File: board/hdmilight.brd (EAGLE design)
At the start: 68.5 x 68.6 mm, 73 parts, among them IC1 REG1117, IC2 REG1117, J1 POWER_JACKPTH, Q1 28.6363MHz

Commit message: fixed value of HDMI pull up resistors on receiver board
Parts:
- R1: value 27R -> 27K
- R2, R3: value 47R -> 1K5
- R7, R8: value 47R -> 47K
- R9: value 100R -> 100K
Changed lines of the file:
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@@
 <attribute name="VALUE" x="49.403" y="9.144" size="1.27" layer="27"/>
 </element>
-<element name="R2" library="resistor" package="R0603" value="47R" x="53.086" y="6.35" smashed="yes">
+<element name="R2" library="resistor" package="R0603" value="1K5" x="53.086" y="6.35" smashed="yes">
 <attribute name="NAME" x="52.197" y="7.747" size="1.016" layer="25"/>
 <attribute name="VALUE" x="52.197" y="4.318" size="1.27" layer="27"/>
 </element>
-<element name="R3" library="resistor" package="R0603" value="47R" x="53.086" y="4.064" smashed="yes">
+<element name="R3" library="resistor" package="R0603" value="1K5" x="53.086" y="4.064" smashed="yes">
 <attribute name="NAME" x="52.451" y="1.651" size="1.016" layer="25"/>
 <attribute name="VALUE" x="52.197" y="2.032" size="1.27" layer="27"/>
 </element>
-<element name="R7" library="resistor" package="R0603" value="47R" x="36.068" y="23.622" smashed="yes" rot="R180">
+<element name="R7" library="resistor" package="R0603" value="47K" x="36.068" y="23.622" smashed="yes" rot="R180">
 <attribute name="NAME" x="37.465" y="22.225" size="1.016" layer="25" rot="R180"/>
 <attribute name="VALUE" x="36.957" y="25.654" size="1.27" layer="27" rot="R180"/>
 </element>
-<element name="R8" library="resistor" package="R0603" value="47R" x="36.068" y="25.654" smashed="yes" rot="R180">
+<element name="R8" library="resistor" package="R0603" value="47K" x="36.068" y="25.654" smashed="yes" rot="R180">
 <attribute name="NAME" x="36.703" y="28.321" size="1.016" layer="25" rot="R180"/>
 <attribute name="VALUE" x="36.957" y="27.686" size="1.27" layer="27" rot="R180"/>
 </element>
-<element name="R1" library="resistor" package="R0603" value="27R" x="35.56" y="13.716" smashed="yes" rot="R180">
+<element name="R1" library="resistor" package="R0603" value="27K" x="35.56" y="13.716" smashed="yes" rot="R180">
 <attribute name="NAME" x="32.639" y="14.605" size="1.016" layer="25" rot="R270"/>
 <attribute name="VALUE" x="36.449" y="15.748" size="1.27" layer="27" rot="R180"/>
 </element>
-<element name="R9" library="resistor" package="R0603" value="100R" x="35.56" y="15.748" smashed="yes" rot="R180">
+<element name="R9" library="resistor" package="R0603" value="100K" x="35.56" y="15.748" smashed="yes" rot="R180">
 <attribute name="NAME" x="32.639" y="16.637" size="1.016" layer="25" rot="R270"/>
 <attribute name="VALUE" x="36.449" y="17.78" size="1.27" layer="27" rot="R180"/>

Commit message: added missing capacitor values to schematic
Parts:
- C15, C16, C17, C18, C19, C20, C21, C22, C23, C24, C25, C26, C33, C34, C35, C36, C37: value (none) -> 0.1uF
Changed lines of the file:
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@@
 </element>
 <element name="U$5" library="__SR" package="TSSOP20" value="TXB0108" x="15.748" y="14.986" rot="R270"/>
-<element name="C22" library="resistor" package="C0603" value="" x="41.656" y="24.384" smashed="yes" rot="MR180">
+<element name="C22" library="resistor" package="C0603" value="0.1uF" x="41.656" y="24.384" smashed="yes" rot="MR180">
 <attribute name="NAME" x="40.005" y="23.114" size="1.016" layer="26" rot="MR180"/>
 <attribute name="VALUE" x="40.767" y="26.416" size="1.27" layer="28" rot="MR180"/>
 </element>
-<element name="C15" library="resistor" package="C0402" value="" x="45.466" y="35.052" smashed="yes" rot="MR180">
+<element name="C15" library="resistor" package="C0402" value="0.1uF" x="45.466" y="35.052" smashed="yes" rot="MR180">
 <attribute name="NAME" x="44.323" y="37.084" size="1.016" layer="26" rot="MR180"/>
 <attribute name="VALUE" x="44.831" y="36.957" size="1.27" layer="28" rot="MR180"/>
 </element>
-<element name="C23" library="resistor" package="C0402" value="" x="46.99" y="32.766" smashed="yes" rot="MR90">
+<element name="C23" library="resistor" package="C0402" value="0.1uF" x="46.99" y="32.766" smashed="yes" rot="MR90">
 <attribute name="NAME" x="48.006" y="31.623" size="1.016" layer="26" rot="MR90"/>
 <attribute name="VALUE" x="45.085" y="32.131" size="1.27" layer="28" rot="MR90"/>
 </element>
-<element name="C34" library="resistor" package="C0402" value="" x="40.386" y="35.052" smashed="yes" rot="MR180">
+<element name="C34" library="resistor" package="C0402" value="0.1uF" x="40.386" y="35.052" smashed="yes" rot="MR180">
 <attribute name="NAME" x="39.243" y="37.084" size="1.016" layer="26" rot="MR180"/>
 <attribute name="VALUE" x="39.751" y="36.957" size="1.27" layer="28" rot="MR180"/>
 </element>
-<element name="C16" library="resistor" package="C0603" value="" x="26.67" y="30.734" smashed="yes" rot="MR270">
+<element name="C16" library="resistor" package="C0603" value="0.1uF" x="26.67" y="30.734" smashed="yes" rot="MR270">
 <attribute name="NAME" x="29.21" y="32.131" size="1.016" layer="26" rot="MR270"/>
 <attribute name="VALUE" x="28.702" y="31.623" size="1.27" layer="28" rot="MR270"/>
 </element>
-<element name="C17" library="resistor" package="C0603" value="" x="40.386" y="41.148" smashed="yes" rot="MR0">
+<element name="C17" library="resistor" package="C0603" value="0.1uF" x="40.386" y="41.148" smashed="yes" rot="MR0">
 <attribute name="NAME" x="41.529" y="42.418" size="1.016" layer="26" rot="MR0"/>
 <attribute name="VALUE" x="41.275" y="39.116" size="1.27" layer="28" rot="MR0"/>
 </element>
-<element name="C24" library="resistor" package="C0603" value="" x="49.276" y="39.624" smashed="yes" rot="MR90">
+<element name="C24" library="resistor" package="C0603" value="0.1uF" x="49.276" y="39.624" smashed="yes" rot="MR90">
 <attribute name="NAME" x="50.546" y="38.481" size="1.016" layer="26" rot="MR90"/>
 <attribute name="VALUE" x="47.244" y="38.735" size="1.27" layer="28" rot="MR90"/>
 </element>
-<element name="C35" library="resistor" package="C0603" value="" x="52.324" y="32.004" smashed="yes" rot="MR90">
+<element name="C35" library="resistor" package="C0603" value="0.1uF" x="52.324" y="32.004" smashed="yes" rot="MR90">
 <attribute name="NAME" x="53.594" y="30.861" size="1.016" layer="26" rot="MR90"/>
 <attribute name="VALUE" x="50.292" y="31.115" size="1.27" layer="28" rot="MR90"/>
 </element>
-<element name="C18" library="resistor" package="C0402" value="" x="40.132" y="27.686" smashed="yes" rot="MR0">
+<element name="C18" library="resistor" package="C0402" value="0.1uF" x="40.132" y="27.686" smashed="yes" rot="MR0">
 <attribute name="NAME" x="41.275" y="25.654" size="1.016" layer="26" rot="MR0"/>
 <attribute name="VALUE" x="40.767" y="25.781" size="1.27" layer="28" rot="MR0"/>
 </element>
-<element name="C19" library="resistor" package="C0603" value="" x="49.276" y="17.272" smashed="yes" rot="MR180">
+<element name="C19" library="resistor" package="C0603" value="0.1uF" x="49.276" y="17.272" smashed="yes" rot="MR180">
 <attribute name="NAME" x="48.133" y="15.748" size="1.016" layer="26" rot="MR180"/>
 <attribute name="VALUE" x="48.387" y="19.304" size="1.27" layer="28" rot="MR180"/>
 </element>
-<element name="C37" library="resistor" package="C0402" value="" x="39.878" y="31.242" smashed="yes" rot="MR90">
+<element name="C37" library="resistor" package="C0402" value="0.1uF" x="39.878" y="31.242" smashed="yes" rot="MR90">
 <attribute name="NAME" x="37.846" y="29.845" size="1.016" layer="26" rot="MR90"/>
 <attribute name="VALUE" x="37.973" y="30.607" size="1.27" layer="28" rot="MR90"/>
 </element>
-<element name="C33" library="resistor" package="C0603" value="" x="44.704" y="23.622" smashed="yes" rot="MR0">
+<element name="C33" library="resistor" package="C0603" value="0.1uF" x="44.704" y="23.622" smashed="yes" rot="MR0">
 <attribute name="NAME" x="46.101" y="21.336" size="1.016" layer="26" rot="MR0"/>
 <attribute name="VALUE" x="45.593" y="21.59" size="1.27" layer="28" rot="MR0"/>
 </element>
-<element name="C25" library="resistor" package="C0402" value="" x="43.688" y="29.21" smashed="yes" rot="MR180">
+<element name="C25" library="resistor" package="C0402" value="0.1uF" x="43.688" y="29.21" smashed="yes" rot="MR180">
 <attribute name="NAME" x="46.355" y="29.718" size="1.016" layer="26" rot="MR180"/>
 <attribute name="VALUE" x="43.053" y="31.115" size="1.27" layer="28" rot="MR180"/>
 </element>
-<element name="C36" library="resistor" package="C0402" value="" x="46.228" y="27.686" smashed="yes" rot="MR180">
+<element name="C36" library="resistor" package="C0402" value="0.1uF" x="46.228" y="27.686" smashed="yes" rot="MR180">
 <attribute name="NAME" x="45.593" y="26.67" size="1.016" layer="26" rot="MR180"/>
 <attribute name="VALUE" x="45.593" y="29.591" size="1.27" layer="28" rot="MR180"/>
@@
 <attribute name="VALUE" x="33.655" y="28.067" size="1.27" layer="27" rot="R180"/>
 </element>
-<element name="C20" library="resistor" package="C0603" value="" x="10.414" y="20.574" smashed="yes" rot="MR90">
+<element name="C20" library="resistor" package="C0603" value="0.1uF" x="10.414" y="20.574" smashed="yes" rot="MR90">
 <attribute name="NAME" x="11.938" y="19.431" size="1.016" layer="26" rot="MR90"/>
 <attribute name="VALUE" x="8.382" y="19.685" size="1.27" layer="28" rot="MR90"/>
 </element>
-<element name="C21" library="resistor" package="C0603" value="" x="20.574" y="19.558" smashed="yes" rot="MR90">
+<element name="C21" library="resistor" package="C0603" value="0.1uF" x="20.574" y="19.558" smashed="yes" rot="MR90">
 <attribute name="NAME" x="22.098" y="18.415" size="1.016" layer="26" rot="MR90"/>
 <attribute name="VALUE" x="18.542" y="18.669" size="1.27" layer="28" rot="MR90"/>
 </element>
-<element name="C26" library="resistor" package="C0603" value="" x="55.372" y="9.906" smashed="yes" rot="MR270">
+<element name="C26" library="resistor" package="C0603" value="0.1uF" x="55.372" y="9.906" smashed="yes" rot="MR270">
 <attribute name="NAME" x="53.848" y="11.049" size="1.016" layer="26" rot="MR270"/>
 <attribute name="VALUE" x="57.404" y="10.795" size="1.27" layer="28" rot="MR270"/>

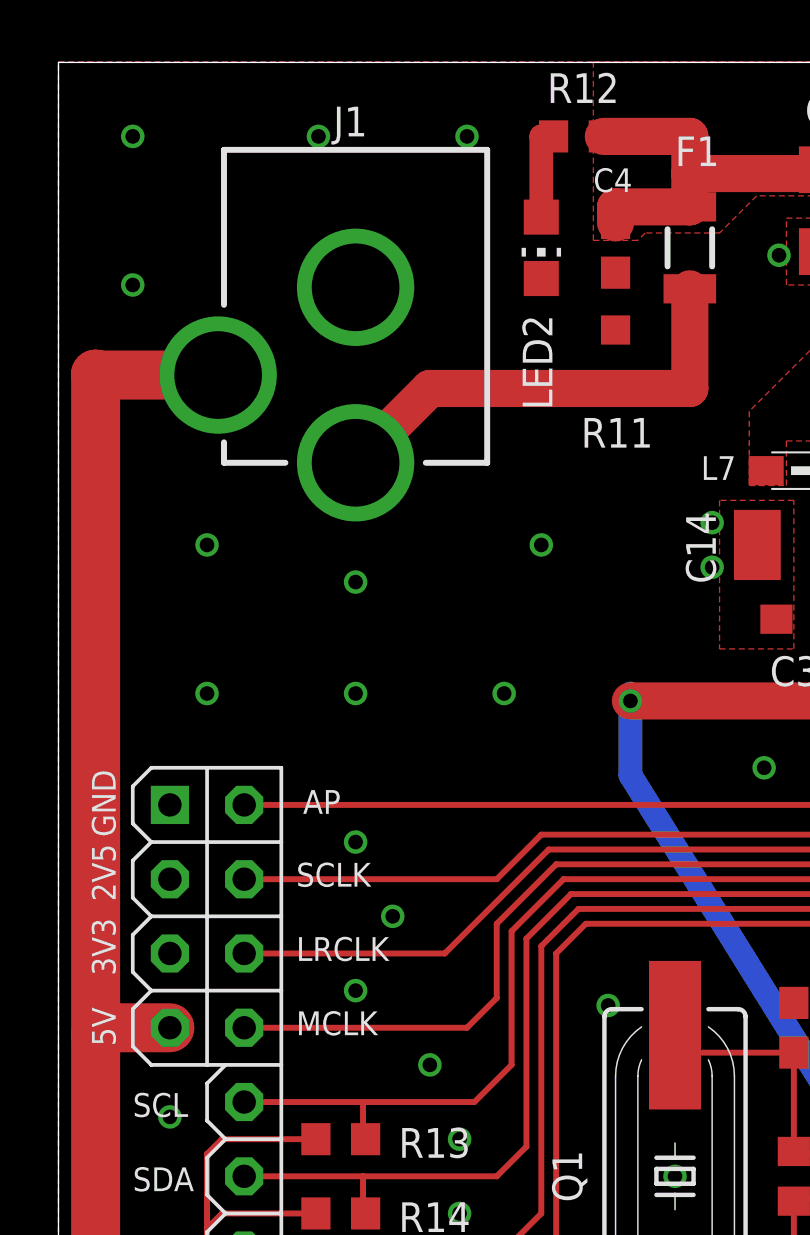
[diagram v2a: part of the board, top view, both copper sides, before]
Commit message: removed power jack from HDMI receiver board
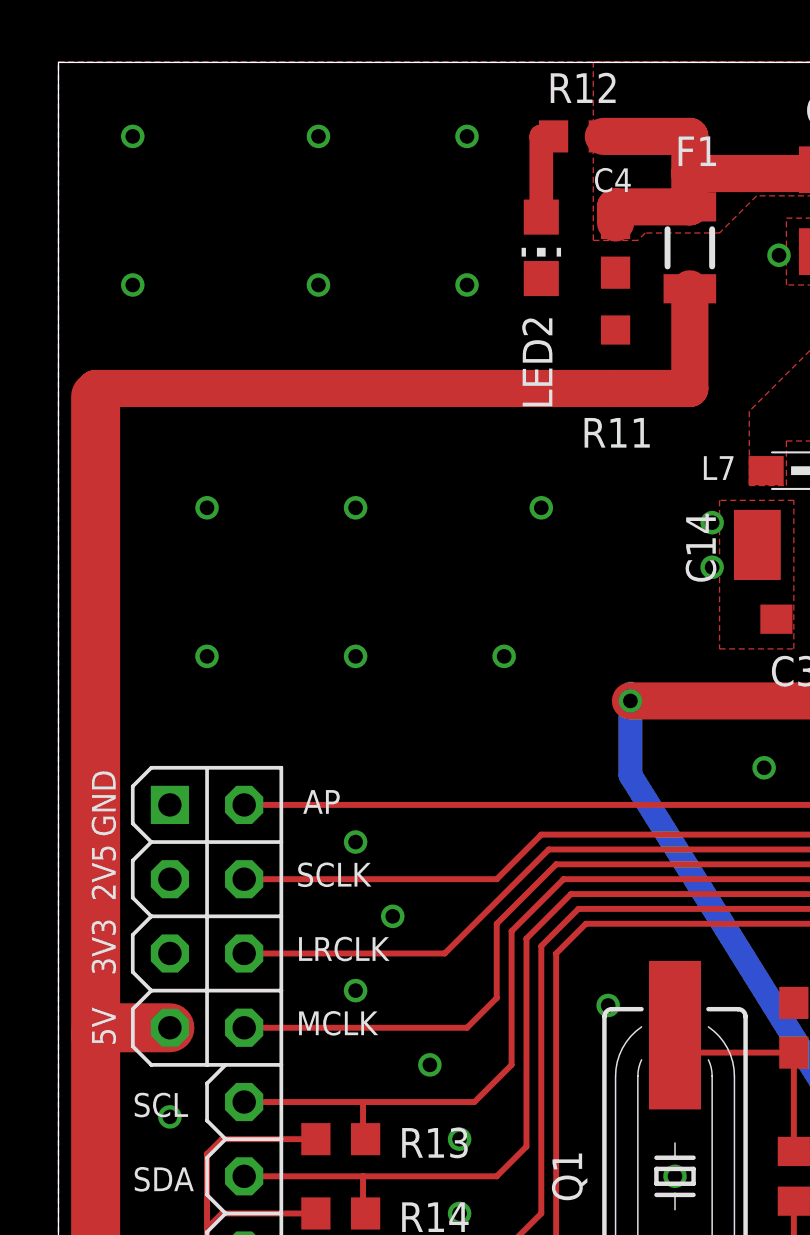
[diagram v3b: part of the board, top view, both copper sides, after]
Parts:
- removed J1: POWER_JACKPTH, SparkFun:POWER_JACK_PTH
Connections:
- removed net N$17: F1.1, J1.PWR, R11.1
- net +5V: now also F1.1, R11.1; no longer J1.GNDBREAK
- net GND: no longer J1.GND
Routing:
- net +5V: track 52.1 -> 71.1 mm
- net N$17: track 15.9 -> 0.00 mm
- net GND: vias 102 -> 104
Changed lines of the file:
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@@
 <setting verticaltext="up"/>
 </settings>
-<grid distance="0.01" unitdist="inch" unit="inch" style="dots" multiple="1" display="yes" altdistance="0.01" altunitdist="inch" altunit="inch"/>
+<grid distance="0.05" unitdist="inch" unit="inch" style="dots" multiple="1" display="yes" altdistance="0.01" altunitdist="inch" altunit="inch"/>
 <layers>
 <layer number="1" name="Top" color="4" fill="1" visible="yes" active="yes"/>
@@
 <attribute name="VALUE" x="40.513" y="60.96" size="1.27" layer="27" rot="R90"/>
 </element>
-<element name="J1" library="SparkFun" package="POWER_JACK_PTH" value="POWER_JACKPTH" x="10.16" y="68.58" smashed="yes" rot="R180">
-<attribute name="NAME" x="9.398" y="66.04" size="1.016" layer="25"/>
-<attribute name="VALUE" x="13.97" y="64.77" size="0.4064" layer="27" rot="R180"/>
-</element>
 <element name="SV1" library="con-lstb" package="MA08-2" value="" x="19.558" y="3.81" smashed="yes">
 <attribute name="OC_NEWARK" value="unknown" x="19.558" y="3.81" size="1.778" layer="27" display="off"/>
@@
 <contactref element="U$7" pad="W3_GND"/>
 <contactref element="U$7" pad="W3_GND_2"/>
-<contactref element="J1" pad="GND"/>
 <polygon width="0.2032" layer="1" thermals="no">
 <vertex x="25.146" y="53.594"/>
@@
 <via x="8.89" y="66.04" extent="1-16" drill="0.5"/>
 <via x="13.97" y="66.04" extent="1-16" drill="0.5"/>
-<via x="5.08" y="52.07" extent="1-16" drill="0.5"/>
-<via x="5.08" y="46.99" extent="1-16" drill="0.5"/>
-<via x="10.16" y="50.8" extent="1-16" drill="0.5"/>
-<via x="10.16" y="46.99" extent="1-16" drill="0.5"/>
-<via x="16.51" y="52.07" extent="1-16" drill="0.5"/>
-<via x="15.24" y="46.99" extent="1-16" drill="0.5"/>
+<via x="5.08" y="53.34" extent="1-16" drill="0.5"/>
+<via x="5.08" y="48.26" extent="1-16" drill="0.5"/>
+<via x="10.16" y="53.34" extent="1-16" drill="0.5"/>
+<via x="10.16" y="48.26" extent="1-16" drill="0.5"/>
+<via x="16.51" y="53.34" extent="1-16" drill="0.5"/>
+<via x="15.24" y="48.26" extent="1-16" drill="0.5"/>
 <via x="24.13" y="44.45" extent="1-16" drill="0.5"/>
 <via x="33.02" y="44.45" extent="1-16" drill="0.5"/>
@@
 <via x="37.338" y="21.844" extent="1-16" drill="0.5"/>
 <via x="7.874" y="21.082" extent="1-16" drill="0.5"/>
+<via x="8.89" y="60.96" extent="1-16" drill="0.5"/>
+<via x="13.97" y="60.96" extent="1-16" drill="0.5"/>
 </signal>
 <signal name="P23">
@@
 <wire x1="38.354" y1="8.526" x2="38.398" y2="8.57" width="0.2032" layer="1"/>
 <wire x1="51.728" y1="4.572" x2="52.236" y2="4.064" width="0.2032" layer="1"/>
-</signal>
-<signal name="N$17">
-<contactref element="F1" pad="1"/>
-<contactref element="R11" pad="1"/>
-<contactref element="J1" pad="PWR"/>
-<wire x1="19.05" y1="57.42" x2="12.7" y2="57.42" width="1.27" layer="1"/>
-<wire x1="12.7" y1="57.42" x2="10.16" y2="54.88" width="1.27" layer="1"/>
-<wire x1="19.05" y1="57.42" x2="21.59" y2="57.42" width="1.27" layer="1"/>
-<wire x1="21.59" y1="57.42" x2="21.59" y2="60.83" width="1.27" layer="1"/>
 </signal>
 <signal name="VCC_5V0">
@@
 </signal>
 <signal name="+5V">
-<contactref element="J1" pad="GNDBREAK"/>
 <contactref element="U$7" pad="W3_5V"/>
 <contactref element="U$7" pad="W3_5V_2"/>
-<wire x1="5.46" y1="57.88" x2="1.302" y2="57.88" width="1.6764" layer="1"/>
-<wire x1="1.302" y1="57.88" x2="1.27" y2="57.912" width="1.6764" layer="1"/>
-<wire x1="1.27" y1="57.912" x2="1.27" y2="35.306" width="1.6764" layer="1"/>
+<wire x1="1.27" y1="57.15" x2="1.27" y2="35.306" width="1.6764" layer="1"/>
 <wire x1="1.27" y1="35.306" x2="1.27" y2="15.24" width="1.6764" layer="1"/>
 <wire x1="1.27" y1="15.24" x2="3.81" y2="15.24" width="1.6764" layer="1"/>
 <wire x1="3.81" y1="35.56" x2="1.524" y2="35.56" width="1.6764" layer="1"/>
 <wire x1="1.524" y1="35.56" x2="1.27" y2="35.306" width="1.6764" layer="1"/>
+<contactref element="F1" pad="1"/>
+<contactref element="R11" pad="1"/>
+<wire x1="19.05" y1="57.42" x2="21.59" y2="57.42" width="1.27" layer="1"/>
+<wire x1="21.59" y1="57.42" x2="21.59" y2="60.83" width="1.27" layer="1"/>
+<wire x1="19.05" y1="57.42" x2="1.27" y2="57.42" width="1.27" layer="1"/>
+<wire x1="1.27" y1="57.42" x2="1.27" y2="57.15" width="1.27" layer="1"/>
 </signal>
 <signal name="N$34">
